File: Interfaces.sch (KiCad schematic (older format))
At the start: 15 parts

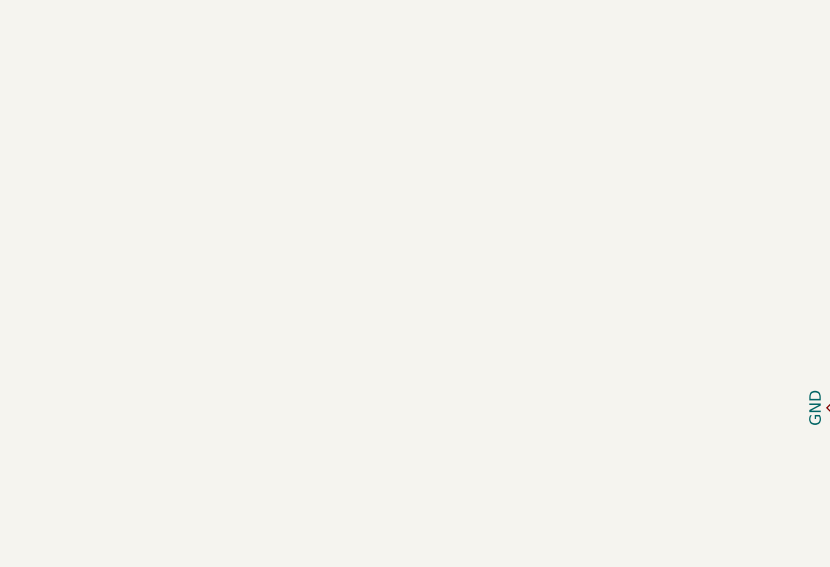
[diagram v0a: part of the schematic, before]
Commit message: Added to scheamtic.
Added reset circuit for Aiya, power led for 3V3 line, USB type A connectors for USBB and USBC.
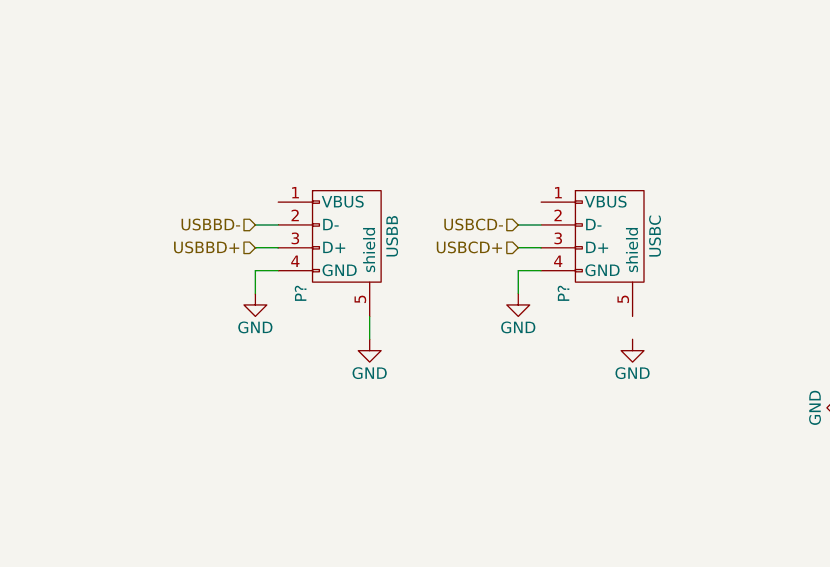
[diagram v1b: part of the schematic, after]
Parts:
- added P?: USBB, symbol USB_A
- added P?: USBC, symbol USB_A
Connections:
- net labels added: USBBD+, USBBD-, USBCD+, USBCD-
- wire segments 79 -> 88
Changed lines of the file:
@@
 LIBS:w_connectors
 LIBS:max-lin
+LIBS:IHE
 LIBS:E-GIF-M-Board-cache
 EELAYER 25 0
@@
 Wire Wire Line
 	1550 6950 1650 6950
+$Comp
+L USB_A P?
+U 1 1 5897E5DB
+P 6200 1900
+F 0 "P?" H 6400 1700 50  0000 C CNN
+F 1 "USBB" H 6150 2100 50  0000 C CNN
+F 2 "" V 6150 1800 50  0000 C CNN
+F 3 "" V 6150 1800 50  0000 C CNN
+	1    6200 1900
+	0    1    1    0
+$EndComp
+$Comp
+L USB_A P?
+U 1 1 5897E6A2
+P 7350 1900
+F 0 "P?" H 7550 1700 50  0000 C CNN
+F 1 "USBC" H 7300 2100 50  0000 C CNN
+F 2 "" V 7300 1800 50  0000 C CNN
+F 3 "" V 7300 1800 50  0000 C CNN
+	1    7350 1900
+	0    1    1    0
+$EndComp
+$Comp
+L GND #PWR?
+U 1 1 5897F3DC
+P 7450 2300
+F 0 "#PWR?" H 7450 2050 50  0001 C CNN
+F 1 "GND" H 7450 2150 50  0000 C CNN
+F 2 "" H 7450 2300 50  0000 C CNN
+F 3 "" H 7450 2300 50  0000 C CNN
+	1    7450 2300
+	1    0    0    -1
+$EndComp
+$Comp
+L GND #PWR?
+U 1 1 5897F6E6
+P 6300 2300
+F 0 "#PWR?" H 6300 2050 50  0001 C CNN
+F 1 "GND" H 6300 2150 50  0000 C CNN
+F 2 "" H 6300 2300 50  0000 C CNN
+F 3 "" H 6300 2300 50  0000 C CNN
+	1    6300 2300
+	1    0    0    -1
+$EndComp
+$Comp
+L GND #PWR?
+U 1 1 5897F8C4
+P 5800 2100
+F 0 "#PWR?" H 5800 1850 50  0001 C CNN
+F 1 "GND" H 5800 1950 50  0000 C CNN
+F 2 "" H 5800 2100 50  0000 C CNN
+F 3 "" H 5800 2100 50  0000 C CNN
+	1    5800 2100
+	1    0    0    -1
+$EndComp
+$Comp
+L GND #PWR?
+U 1 1 5897F944
+P 6950 2100
+F 0 "#PWR?" H 6950 1850 50  0001 C CNN
+F 1 "GND" H 6950 1950 50  0000 C CNN
+F 2 "" H 6950 2100 50  0000 C CNN
+F 3 "" H 6950 2100 50  0000 C CNN
+	1    6950 2100
+	1    0    0    -1
+$EndComp
+Wire Wire Line
+	5800 2100 5800 2000
+Wire Wire Line
+	5800 2000 5900 2000
+Wire Wire Line
+	6950 2100 6950 2000
+Wire Wire Line
+	6950 2000 7050 2000
+Text HLabel 5800 1800 0    50   Input ~ 0
+USBBD-
+Text HLabel 5800 1900 0    50   Input ~ 0
+USBBD+
+Wire Wire Line
+	5800 1800 5900 1800
+Wire Wire Line
+	5800 1900 5900 1900
+Wire Wire Line
+	6300 2200 6300 2300
+Text HLabel 6950 1800 0    50   Input ~ 0
+USBCD-
+Text HLabel 6950 1900 0    50   Input ~ 0
+USBCD+
+Wire Wire Line
+	6950 1800 7050 1800
+Wire Wire Line
+	6950 1900 7050 1900
 $EndSCHEMATC

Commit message: Schematic correction
Corrected the direction on some signals. Added a pin header for general development.
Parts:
- added W2: U2S_RST, symbol TEST_1P
- added W3: RX_T, symbol TEST_1P
- added W4: TX_T, symbol TEST_1P
- C19, C20, C21, C22, C23, C24: renamed from C?; footprint (none) -> Capacitors_SMD:C_0603_HandSoldering
- P4: renamed from P?; value USB_OTG -> DEBUG
- R4, R5: renamed from R?; footprint (none) -> Resistors_SMD:R_0603_HandSoldering
- gave numbers to parts that had none: 8
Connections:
- net labels added: TCT
- net labels removed: CTC, VUSB
- wire segments 88 -> 91
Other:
- moved on the sheet: C21, C22, C23, C24, D4, D5, P2, P3, P4, R4, R5, U3

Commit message: Modified LAN9500A schematic.
Modified the schematic for the USB to Ethernet converter.
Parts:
- C19, C20, C21, C22, C23, C24: footprint Capacitors_SMD:C_0603_HandSoldering -> Capacitors_SMD:C_0805_HandSoldering
- D4, D5: footprint (none) -> LEDs:LED_0805
- J2: footprint (none) -> Connectors:RJ45_TRANSFO
- R4, R5: footprint Resistors_SMD:R_0603_HandSoldering -> Resistors_SMD:R_0805_HandSoldering
- Y1: footprint (none) -> Crystals:Crystal_SMD_3225-4pin_3.2x2.5mm_HandSoldering
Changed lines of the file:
@@
 $Descr A4 11693 8268
 encoding utf-8
-Sheet 3 7
+Sheet 4 7
 Title ""
 Date ""
@@
 F 0 "C20" H 1425 3800 50  0000 L CNN
 F 1 "1uF" V 1350 3500 50  0000 L CNN
-F 2 "Capacitors_SMD:C_0603_HandSoldering" H 1438 3550 50  0001 C CNN
+F 2 "Capacitors_SMD:C_0805_HandSoldering" H 1438 3550 50  0001 C CNN
 F 3 "" H 1400 3700 50  0000 C CNN
 	1    1400 3700
@@
 F 0 "C19" H 1225 3800 50  0000 L CNN
 F 1 "100nF" V 1150 3400 50  0000 L CNN
-F 2 "Capacitors_SMD:C_0603_HandSoldering" H 1238 3550 50  0001 C CNN
+F 2 "Capacitors_SMD:C_0805_HandSoldering" H 1238 3550 50  0001 C CNN
 F 3 "" H 1200 3700 50  0000 C CNN
 	1    1200 3700
@@
 F 0 "C22" H 9125 1450 50  0000 L CNN
 F 1 "1uF" V 9050 1150 50  0000 L CNN
-F 2 "Capacitors_SMD:C_0603_HandSoldering" H 9138 1200 50  0001 C CNN
+F 2 "Capacitors_SMD:C_0805_HandSoldering" H 9138 1200 50  0001 C CNN
 F 3 "" H 9100 1350 50  0000 C CNN
 	1    9100 1350
@@
 F 0 "C21" H 9125 1200 50  0000 L CNN
 F 1 "100nF" V 9050 800 50  0000 L CNN
-F 2 "Capacitors_SMD:C_0603_HandSoldering" H 9138 950 50  0001 C CNN
+F 2 "Capacitors_SMD:C_0805_HandSoldering" H 9138 950 50  0001 C CNN
 F 3 "" H 9100 1100 50  0000 C CNN
 	1    9100 1100
@@
 F 0 "Y1" H 9400 4150 50  0000 L CNN
 F 1 "12MHz" H 9250 3750 50  0000 L CNN
-F 2 "" H 9550 3950 50  0001 C CNN
+F 2 "Crystals:Crystal_SMD_3225-4pin_3.2x2.5mm_HandSoldering" H 9550 3950 50  0001 C CNN
 F 3 "" H 9550 3950 50  0000 C CNN
 	1    9550 3950
@@
 F 0 "C24" H 9925 4300 50  0000 L CNN
 F 1 "6pF" H 9750 4100 50  0000 L CNN
-F 2 "Capacitors_SMD:C_0603_HandSoldering" H 9938 4050 50  0001 C CNN
+F 2 "Capacitors_SMD:C_0805_HandSoldering" H 9938 4050 50  0001 C CNN
 F 3 "" H 9900 4200 50  0000 C CNN
 	1    9900 4200
@@
 F 0 "C23" H 9225 4300 50  0000 L CNN
 F 1 "6pF" H 9050 4100 50  0000 L CNN
-F 2 "Capacitors_SMD:C_0603_HandSoldering" H 9238 4050 50  0001 C CNN
+F 2 "Capacitors_SMD:C_0805_HandSoldering" H 9238 4050 50  0001 C CNN
 F 3 "" H 9200 4200 50  0000 C CNN
 	1    9200 4200
@@
 F 0 "R4" V 8500 2550 50  0000 C CNN
 F 1 "R" V 8600 2550 50  0000 C CNN
-F 2 "Resistors_SMD:R_0603_HandSoldering" V 8530 2550 50  0001 C CNN
+F 2 "Resistors_SMD:R_0805_HandSoldering" V 8530 2550 50  0001 C CNN
 F 3 "" H 8600 2550 50  0000 C CNN
 	1    8600 2550
@@
 F 0 "R5" V 8700 2650 50  0000 C CNN
 F 1 "R" V 8600 2650 50  0000 C CNN
-F 2 "Resistors_SMD:R_0603_HandSoldering" V 8530 2650 50  0001 C CNN
+F 2 "Resistors_SMD:R_0805_HandSoldering" V 8530 2650 50  0001 C CNN
 F 3 "" H 8600 2650 50  0000 C CNN
 	1    8600 2650
@@
 F 0 "D4" H 8150 2600 50  0000 C CNN
 F 1 "LED" H 8300 2600 50  0000 C CNN
-F 2 "" H 8200 2500 50  0001 C CNN
+F 2 "LEDs:LED_0805" H 8200 2500 50  0001 C CNN
 F 3 "" H 8200 2500 50  0000 C CNN
 	1    8200 2500
@@
 F 0 "D5" H 8100 2550 50  0000 C CNN
 F 1 "LED" H 8300 2550 50  0000 C CNN
-F 2 "" H 8200 2700 50  0001 C CNN
+F 2 "LEDs:LED_0805" H 8200 2700 50  0001 C CNN
 F 3 "" H 8200 2700 50  0000 C CNN
 	1    8200 2700
@@
 F 0 "J2" H 3100 2100 50  0000 L CNN
 F 1 "RJ45-TRANSFO-ACME" H 2950 2100 50  0000 R CNN
-F 2 "" H 3000 1500 50  0001 C CNN
+F 2 "Connectors:RJ45_TRANSFO" H 3000 1500 50  0001 C CNN
 F 3 "" H 3000 1500 50  0000 C CNN
 	1    3000 1500
@@
 F1 "USB_ETH_conv.sch" 60
 F2 "nRESET" I R 1550 5150 50
-F3 "USBD-" I R 1550 5250 50
-F4 "USBD+" I R 1550 5350 50
+F3 "USBDP" B R 1550 5350 50
+F4 "USBDM" B R 1550 5250 50
 $EndSheet
 Text HLabel 1650 5150 2    50   Input ~ 0

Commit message: Schematic changes. PCB in process of making.
Removed LAN9500A Jtag. Removed Aria G25 pinout. Removed USB connectors. Added rezistors to USB/ETH/ySD shields.
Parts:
- removed J2: RJ45-TRANSFO-ACME, Connectors:RJ45_TRANSFO, symbol RJ45-TRANSFO-ACME
- removed P2: USBB, symbol USB_A
- removed P3: USBC, symbol USB_A
- removed Y1: 12MHz, Crystals:Crystal_SMD_3225-4pin_3.2x2.5mm_HandSoldering, symbol Crystal_GND23
- added J2: RJ45-TRANSFO, Connectors:RJ45_TRANSFO, symbol RJ45-TRANSFO
- added R15, R16, R19: 1M, Resistors_SMD:R_0805_HandSoldering, symbol R
- added Y1: 16MHz, Crystals:Crystal_SMD_3225-4pin_3.2x2.5mm_HandSoldering, symbol Crystal_GND24
- CON2: footprint (none) -> Custom:MicroSDSocket
- P4: footprint (none) -> Custom:MicroUSB-B
- U3: footprint (none) -> Housings_SSOP:SSOP-20_5.3x7.2mm_Pitch0.65mm
- W2: footprint (none) -> Measurement_Points:Measurement_Point_Round-SMD-Pad_Small
- W3, W4: footprint (none) -> Pin_Headers:Pin_Header_Straight_1x01_Pitch2.54mm
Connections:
- net labels added: VBUS
- net labels removed: USBBD+, USBBD-, USBCD+, USBCD-
- wire segments 91 -> 85
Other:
- note added: "<- +condensator?"

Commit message: Modified USB/ETH label names.
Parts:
- R15, R16, R19, R4, R5: footprint Resistors_SMD:R_0805_HandSoldering -> Resistors_SMD:R_0603_HandSoldering
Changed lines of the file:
@@
 F 0 "R4" V 8500 2550 50  0000 C CNN
 F 1 "R" V 8600 2550 50  0000 C CNN
-F 2 "Resistors_SMD:R_0805_HandSoldering" V 8530 2550 50  0001 C CNN
+F 2 "Resistors_SMD:R_0603_HandSoldering" V 8530 2550 50  0001 C CNN
 F 3 "" H 8600 2550 50  0000 C CNN
 	1    8600 2550
@@
 F 0 "R5" V 8700 2650 50  0000 C CNN
 F 1 "R" V 8600 2650 50  0000 C CNN
-F 2 "Resistors_SMD:R_0805_HandSoldering" V 8530 2650 50  0001 C CNN
+F 2 "Resistors_SMD:R_0603_HandSoldering" V 8530 2650 50  0001 C CNN
 F 3 "" H 8600 2650 50  0000 C CNN
 	1    8600 2650
@@
 F1 "USB_ETH_conv.sch" 60
 F2 "nRESET" I R 1550 5150 50
-F3 "USBDP" B R 1550 5350 50
-F4 "USBDM" B R 1550 5250 50
+F3 "USBD_P" B R 1550 5350 50
+F4 "USBD_N" B R 1550 5250 50
 $EndSheet
 Text HLabel 1650 5150 2    50   Input ~ 0
@@
 F 0 "R19" V 9830 5900 50  0000 C CNN
 F 1 "1M" V 9750 5900 50  0000 C CNN
-F 2 "Resistors_SMD:R_0805_HandSoldering" V 9680 5900 50  0001 C CNN
+F 2 "Resistors_SMD:R_0603_HandSoldering" V 9680 5900 50  0001 C CNN
 F 3 "" H 9750 5900 50  0000 C CNN
 	1    9750 5900
@@
 F 0 "R16" V 4230 4050 50  0000 C CNN
 F 1 "1M" V 4150 4050 50  0000 C CNN
-F 2 "Resistors_SMD:R_0805_HandSoldering" V 4080 4050 50  0001 C CNN
+F 2 "Resistors_SMD:R_0603_HandSoldering" V 4080 4050 50  0001 C CNN
 F 3 "" H 4150 4050 50  0000 C CNN
 	1    4150 4050
@@
 F 0 "R15" V 3930 1900 50  0000 C CNN
 F 1 "1M" V 3850 1900 50  0000 C CNN
-F 2 "Resistors_SMD:R_0805_HandSoldering" V 3780 1900 50  0001 C CNN
+F 2 "Resistors_SMD:R_0603_HandSoldering" V 3780 1900 50  0001 C CNN
 F 3 "" H 3850 1900 50  0000 C CNN
 	1    3850 1900

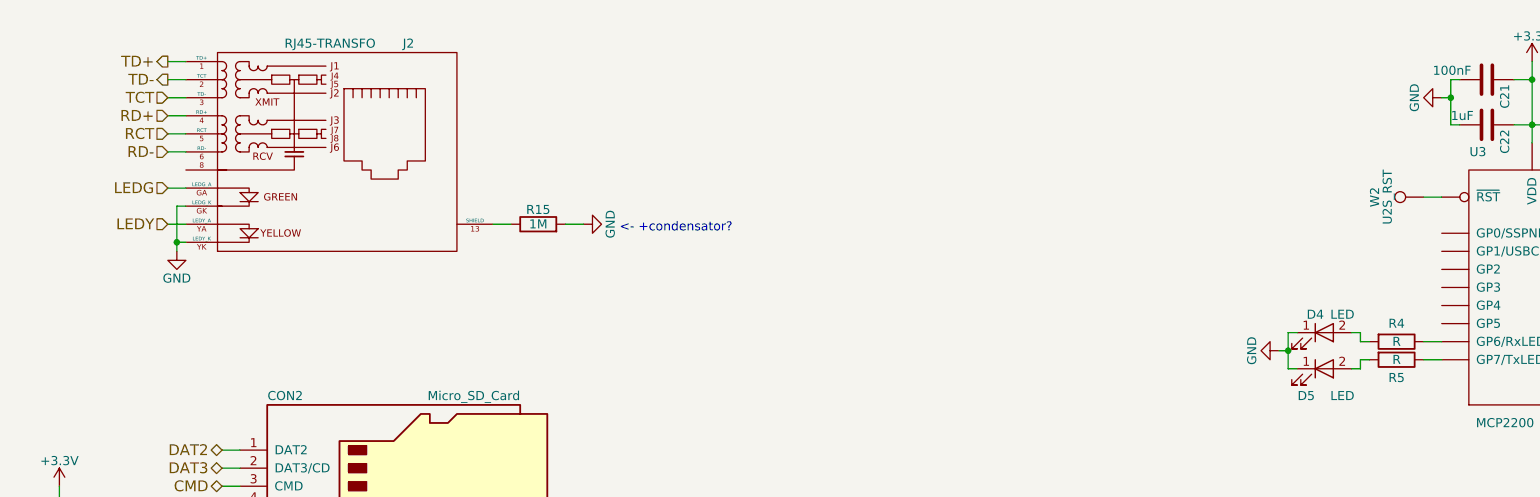
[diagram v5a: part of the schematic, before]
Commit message: Finished first version of PCB.
Modified RJ45 footprint.
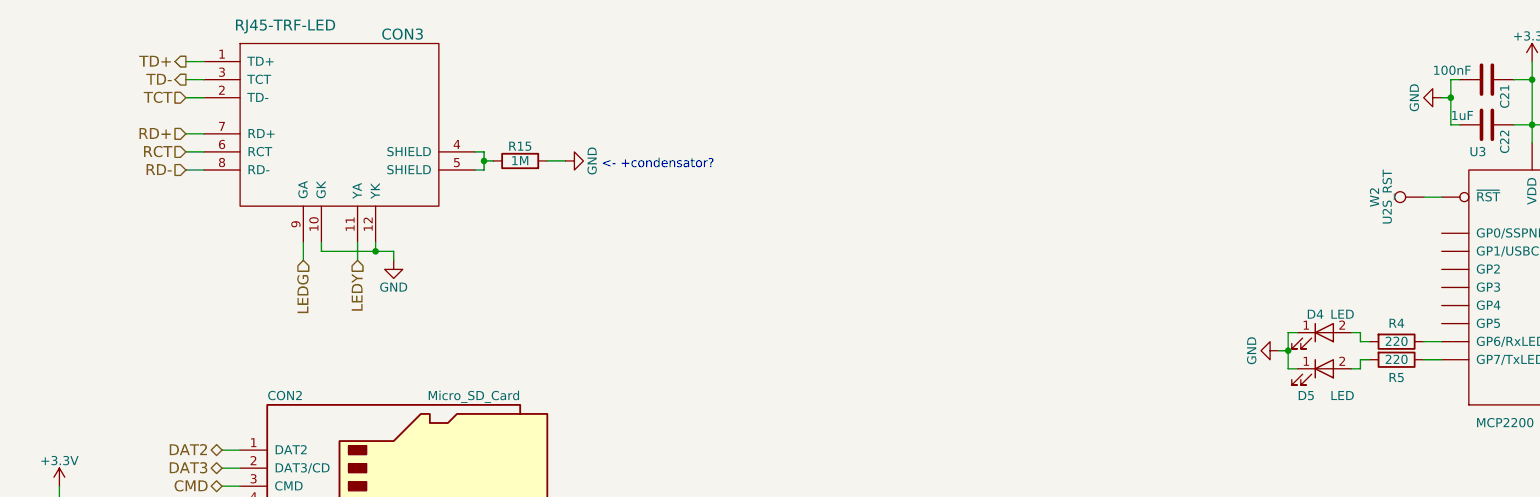
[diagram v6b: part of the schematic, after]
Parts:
- removed J2: RJ45-TRANSFO, Connectors:RJ45_TRANSFO, symbol RJ45-TRANSFO
- added CON3: RJ45-TRF-LED, misc:RJ45_TRANSFO, symbol RJ45-TRF-LED
- R4, R5: value R -> 220
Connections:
- net GND: now also CON3.10 (GK), CON3.12 (YK)
- net LEDG: now also CON3.9 (GA)
- net LEDY: now also CON3.11 (YA)
- net RCT: now also CON3.6 (RCT)
- net RD+: now also CON3.7 (RD+)
- net RD-: now also CON3.8 (RD-)
- net TCT: now also CON3.2 (TD-)
- net TD+: now also CON3.1 (TD+)
- net TD-: now also CON3.3 (TCT)
- net at R15.1: now also CON3.4 (SHIELD), CON3.5 (SHIELD)
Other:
- moved on the sheet: R15
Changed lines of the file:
@@
 P 8600 2550
 F 0 "R4" V 8500 2550 50  0000 C CNN
-F 1 "R" V 8600 2550 50  0000 C CNN
+F 1 "220" V 8600 2550 50  0000 C CNN
 F 2 "Resistors_SMD:R_0603_HandSoldering" V 8530 2550 50  0001 C CNN
 F 3 "" H 8600 2550 50  0000 C CNN
@@
 P 8600 2650
 F 0 "R5" V 8700 2650 50  0000 C CNN
-F 1 "R" V 8600 2650 50  0000 C CNN
+F 1 "220" V 8600 2650 50  0000 C CNN
 F 2 "Resistors_SMD:R_0603_HandSoldering" V 8530 2650 50  0001 C CNN
 F 3 "" H 8600 2650 50  0000 C CNN
@@
 L GND #PWR041
 U 1 1 587FF426
-P 1850 2050
-F 0 "#PWR041" H 1850 1800 50  0001 C CNN
-F 1 "GND" H 1850 1900 50  0000 C CNN
-F 2 "" H 1850 2050 50  0000 C CNN
-F 3 "" H 1850 2050 50  0000 C CNN
-	1    1850 2050
+P 3050 2100
+F 0 "#PWR041" H 3050 1850 50  0001 C CNN
+F 1 "GND" H 3050 1950 50  0000 C CNN
+F 2 "" H 3050 2100 50  0000 C CNN
+F 3 "" H 3050 2100 50  0000 C CNN
+	1    3050 2100
 	1    0    0    -1
 $EndComp
@@
 Text HLabel 10550 2400 2    60   Output ~ 0
 TX
-Text HLabel 1800 1300 0    60   Input ~ 0
+Text HLabel 1900 1400 0    60   Input ~ 0
 RD+
-Text HLabel 1800 1400 0    60   Input ~ 0
+Text HLabel 1900 1500 0    60   Input ~ 0
 RCT
-Text HLabel 1800 1500 0    60   Input ~ 0
+Text HLabel 1900 1600 0    60   Input ~ 0
 RD-
-Text HLabel 1800 1000 0    60   Output ~ 0
+Text HLabel 1900 1000 0    60   Output ~ 0
 TD+
-Text HLabel 1800 1200 0    60   Input ~ 0
+Text HLabel 1900 1200 0    60   Input ~ 0
 TCT
-Text HLabel 1800 1100 0    60   Output ~ 0
+Text HLabel 1900 1100 0    60   Output ~ 0
 TD-
-Text HLabel 1800 1700 0    60   Input ~ 0
+Text HLabel 2550 2100 3    60   Input ~ 0
 LEDG
-Text HLabel 1800 1900 0    60   Input ~ 0
+Text HLabel 2850 2100 3    60   Input ~ 0
 LEDY
 $Sheet
@@
 	8750 2650 8850 2650
 Wire Wire Line
-	1900 1800 1850 1800
-Wire Wire Line
-	1850 1800 1850 2050
-Wire Wire Line
-	1850 2000 1900 2000
-Connection ~ 1850 2000
-Wire Wire Line
 	2100 3150 2200 3150
 Wire Wire Line
@@
 Wire Wire Line
 	10050 2400 10550 2400
-Wire Wire Line
-	1800 1000 1900 1000
-Wire Wire Line
-	1800 1100 1900 1100
-Wire Wire Line
-	1800 1200 1900 1200
-Wire Wire Line
-	1800 1300 1900 1300
-Wire Wire Line
-	1800 1400 1900 1400
-Wire Wire Line
-	1800 1500 1900 1500
-Wire Wire Line
-	1800 1900 1900 1900
-Wire Wire Line
-	1800 1700 1900 1700
 Wire Wire Line
 	1550 5150 1650 5150
@@
 	8750 1750 8850 1750
 $Comp
-L RJ45-TRANSFO J2
-U 1 1 58AAFDCD
-P 3000 1500
-F 0 "J2" H 3100 2100 50  0000 L CNN
-F 1 "RJ45-TRANSFO" H 2950 2100 50  0000 R CNN
-F 2 "Connectors:RJ45_TRANSFO" H 3000 1500 50  0001 C CNN
-F 3 "" H 3000 1500 50  0000 C CNN
-	1    3000 1500
-	1    0    0    -1
-$EndComp
-$Comp
 L GND #PWR042
 U 1 1 58AB20AE
-P 4100 1900
-F 0 "#PWR042" H 4100 1650 50  0001 C CNN
-F 1 "GND" H 4100 1750 50  0000 C CNN
-F 2 "" H 4100 1900 50  0000 C CNN
-F 3 "" H 4100 1900 50  0000 C CNN
-	1    4100 1900
+P 4000 1550
+F 0 "#PWR042" H 4000 1300 50  0001 C CNN
+F 1 "GND" H 4000 1400 50  0000 C CNN
+F 2 "" H 4000 1550 50  0000 C CNN
+F 3 "" H 4000 1550 50  0000 C CNN
+	1    4000 1550
 	0    -1   -1   0
 $EndComp
@@
 L R R15
 U 1 1 58AEC233
-P 3850 1900
-F 0 "R15" V 3930 1900 50  0000 C CNN
-F 1 "1M" V 3850 1900 50  0000 C CNN
-F 2 "Resistors_SMD:R_0603_HandSoldering" V 3780 1900 50  0001 C CNN
-F 3 "" H 3850 1900 50  0000 C CNN
-	1    3850 1900
+P 3750 1550
+F 0 "R15" V 3830 1550 50  0000 C CNN
+F 1 "1M" V 3750 1550 50  0000 C CNN
+F 2 "Resistors_SMD:R_0603_HandSoldering" V 3680 1550 50  0001 C CNN
+F 3 "" H 3750 1550 50  0000 C CNN
+	1    3750 1550
 	0    -1   -1   0
 $EndComp
 Wire Wire Line
-	4100 1900 4000 1900
-Wire Wire Line
-	3700 1900 3600 1900
-Text Notes 4300 1950 0    50   ~ 0
+	4000 1550 3900 1550
+Text Notes 4200 1600 0    50   ~ 0
 <- +condensator?
+$Comp
+L RJ45-TRF-LED CON3
+U 1 1 58B3DF4C
+P 2450 1700
+F 0 "CON3" H 3100 2550 60  0000 C CNN
+F 1 "RJ45-TRF-LED" H 2450 2600 60  0000 C CNN
+F 2 "misc:RJ45_TRANSFO" H 2450 1700 60  0001 C CNN
+F 3 "" H 2450 1700 60  0001 C CNN
+	1    2450 1700
+	1    0    0    -1
+$EndComp
+Wire Wire Line
+	3050 2050 3050 2100
+Wire Wire Line
+	2650 2050 3050 2050
+Wire Wire Line
+	2950 2050 2950 2000
+Wire Wire Line
+	2650 2050 2650 2000
+Connection ~ 2950 2050
+Wire Wire Line
+	2850 2100 2850 2000
+Wire Wire Line
+	2550 2100 2550 2000
+Wire Wire Line
+	1900 1000 2000 1000
+Wire Wire Line
+	1900 1100 2000 1100
+Wire Wire Line
+	1900 1200 2000 1200
+Wire Wire Line
+	1900 1400 2000 1400
+Wire Wire Line
+	1900 1500 2000 1500
+Wire Wire Line
+	1900 1600 2000 1600
+Wire Wire Line
+	3500 1500 3550 1500
+Wire Wire Line
+	3550 1500 3550 1600
+Wire Wire Line
+	3550 1550 3600 1550
+Wire Wire Line
+	3550 1600 3500 1600
+Connection ~ 3550 1550
 $EndSCHEMATC

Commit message: Modified buck circuit on board.
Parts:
- C19, C20, C21, C22, C23, C24: footprint Capacitors_SMD:C_0805_HandSoldering -> Capacitors_SMD:C_0603_HandSoldering
- D4, D5: footprint LEDs:LED_0805 -> LEDs:LED_0603
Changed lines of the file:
@@
 F 0 "C20" H 1425 3800 50  0000 L CNN
 F 1 "1uF" V 1350 3500 50  0000 L CNN
-F 2 "Capacitors_SMD:C_0805_HandSoldering" H 1438 3550 50  0001 C CNN
+F 2 "Capacitors_SMD:C_0603_HandSoldering" H 1438 3550 50  0001 C CNN
 F 3 "" H 1400 3700 50  0000 C CNN
 	1    1400 3700
@@
 F 0 "C19" H 1225 3800 50  0000 L CNN
 F 1 "100nF" V 1150 3400 50  0000 L CNN
-F 2 "Capacitors_SMD:C_0805_HandSoldering" H 1238 3550 50  0001 C CNN
+F 2 "Capacitors_SMD:C_0603_HandSoldering" H 1238 3550 50  0001 C CNN
 F 3 "" H 1200 3700 50  0000 C CNN
 	1    1200 3700
@@
 F 0 "C22" H 9125 1450 50  0000 L CNN
 F 1 "1uF" V 9050 1150 50  0000 L CNN
-F 2 "Capacitors_SMD:C_0805_HandSoldering" H 9138 1200 50  0001 C CNN
+F 2 "Capacitors_SMD:C_0603_HandSoldering" H 9138 1200 50  0001 C CNN
 F 3 "" H 9100 1350 50  0000 C CNN
 	1    9100 1350
@@
 F 0 "C21" H 9125 1200 50  0000 L CNN
 F 1 "100nF" V 9050 800 50  0000 L CNN
-F 2 "Capacitors_SMD:C_0805_HandSoldering" H 9138 950 50  0001 C CNN
+F 2 "Capacitors_SMD:C_0603_HandSoldering" H 9138 950 50  0001 C CNN
 F 3 "" H 9100 1100 50  0000 C CNN
 	1    9100 1100
@@
 F 0 "C24" H 9925 4300 50  0000 L CNN
 F 1 "6pF" H 9750 4100 50  0000 L CNN
-F 2 "Capacitors_SMD:C_0805_HandSoldering" H 9938 4050 50  0001 C CNN
+F 2 "Capacitors_SMD:C_0603_HandSoldering" H 9938 4050 50  0001 C CNN
 F 3 "" H 9900 4200 50  0000 C CNN
 	1    9900 4200
@@
 F 0 "C23" H 9225 4300 50  0000 L CNN
 F 1 "6pF" H 9050 4100 50  0000 L CNN
-F 2 "Capacitors_SMD:C_0805_HandSoldering" H 9238 4050 50  0001 C CNN
+F 2 "Capacitors_SMD:C_0603_HandSoldering" H 9238 4050 50  0001 C CNN
 F 3 "" H 9200 4200 50  0000 C CNN
 	1    9200 4200
@@
 F 0 "D4" H 8150 2600 50  0000 C CNN
 F 1 "LED" H 8300 2600 50  0000 C CNN
-F 2 "LEDs:LED_0805" H 8200 2500 50  0001 C CNN
+F 2 "LEDs:LED_0603" H 8200 2500 50  0001 C CNN
 F 3 "" H 8200 2500 50  0000 C CNN
 	1    8200 2500
@@
 F 0 "D5" H 8100 2550 50  0000 C CNN
 F 1 "LED" H 8300 2550 50  0000 C CNN
-F 2 "LEDs:LED_0805" H 8200 2700 50  0001 C CNN
+F 2 "LEDs:LED_0603" H 8200 2700 50  0001 C CNN
 F 3 "" H 8200 2700 50  0000 C CNN
 	1    8200 2700
